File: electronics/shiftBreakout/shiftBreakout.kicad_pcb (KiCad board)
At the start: 2 copper layers, 94 x 49.5 mm, 45 parts, among them J1 Screw_Terminal_01x05, J10 Sensor C, J11 Sensor D, J2 Screw_Terminal_01x06, J3 Motor A, J4 Screw_Terminal_01x05, J5 Motor B, J6 Motor C, J7 Motor D, J8 Sensor A, J9 Sensor B, U1 74HC595, U2 TPL7407L, U3 74HC244, U4 74HC165, U5 74HC595, U6 TPL7407L, U7 74HC595, U8 TPL7407L

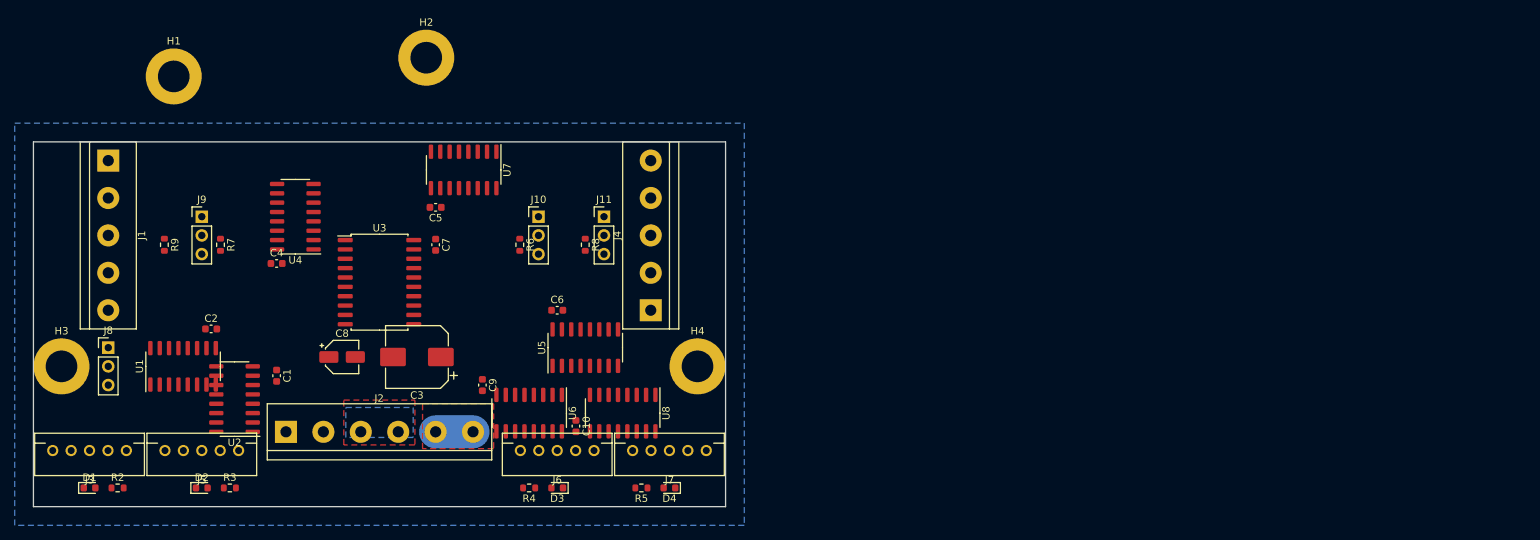
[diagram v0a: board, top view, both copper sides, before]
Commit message: Shift breakout PCB progress
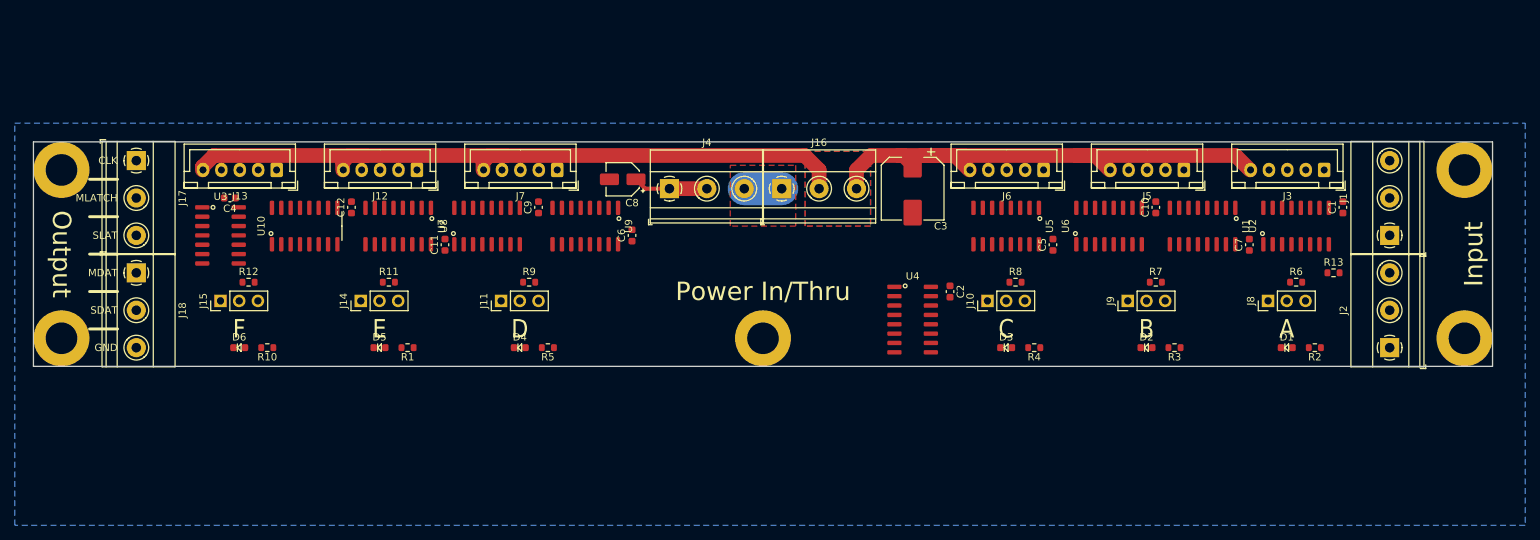
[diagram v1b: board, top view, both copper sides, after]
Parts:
- added C11: 0.1uF, Capacitor_SMD:C_0603_1608Metric, F.Cu at (81.3, 39.4)
- added C12: 0.1uF, Capacitor_SMD:C_0603_1608Metric, F.Cu at (68.6, 34.3)
- added D5: LED E, ModifiedSymbols:LED_0603_1608Metric_Silkscreen, F.Cu at (72.4, 53.3)
- added D6: LED F, ModifiedSymbols:LED_0603_1608Metric_Silkscreen, F.Cu at (53.3, 53.3)
- added H5: MountingHole, MountingHole:MountingHole_4.3mm_M4_ISO7380_Pad, F.Cu at (124.5, 52.1)
- added J12: Motor E, Connector_JST:JST_XH_B5B-XH-A_1x05_P2.50mm_Vertical, F.Cu at (77.5, 29.2)
- added J13: Motor F, Connector_JST:JST_XH_B5B-XH-A_1x05_P2.50mm_Vertical, F.Cu at (58.4, 29.2)
- added J14: Sensor E, Connector_PinHeader_2.54mm:PinHeader_1x03_P2.54mm_Vertical, F.Cu at (69.8, 47.0)
- added J15: Sensor F, Connector_PinHeader_2.54mm:PinHeader_1x03_P2.54mm_Vertical, F.Cu at (50.8, 47.0)
- added J16: PowerB, TerminalBlock_Phoenix:TerminalBlock_Phoenix_MKDS-1,5-3-5.08_1x03_P5.08mm_Horizontal, F.Cu at (127.0, 31.8)
- added J17: Outputs_A, TerminalBlock_Phoenix:TerminalBlock_Phoenix_MKDS-1,5-3-5.08_1x03_P5.08mm_Horizontal, F.Cu at (39.4, 27.9)
- added J18: Outputs_B, TerminalBlock_Phoenix:TerminalBlock_Phoenix_MKDS-1,5-3-5.08_1x03_P5.08mm_Horizontal, F.Cu at (39.4, 43.2)
- added R1: 220R, Resistor_SMD:R_0603_1608Metric, F.Cu at (76.2, 53.3)
- added R10: 220R, Resistor_SMD:R_0603_1608Metric, F.Cu at (57.1, 53.3)
- added R11: 47k, Resistor_SMD:R_0603_1608Metric, F.Cu at (73.7, 44.5)
- added R12: 47k, Resistor_SMD:R_0603_1608Metric, F.Cu at (54.6, 44.5)
- added R13: 0R, Resistor_SMD:R_0603_1608Metric, F.Cu at (201.9, 43.2)
- added U10: TPL7407L, ModifiedSymbols:SOIC-16_3.9x9.9mm_P1.27mm_silk, F.Cu at (62.2, 36.8)
- added U9: 74HC595, ModifiedSymbols:SOIC-16_3.9x9.9mm_P1.27mm_silk, F.Cu at (100.3, 36.8)
- D1, D2, D3, D4: footprint LED_SMD:LED_0603_1608Metric -> ModifiedSymbols:LED_0603_1608Metric_Silkscreen
- J1: value Screw_Terminal_01x05 -> Inputs_B; footprint TerminalBlock:TerminalBlock_bornier-5_P5.08mm -> TerminalBlock_Phoenix:TerminalBlock_Phoenix_MKDS-1,5-3-5.08_1x03_P5.08mm_Horizontal
- J2: value Screw_Terminal_01x06 -> Input_A; footprint TerminalBlock:TerminalBlock_bornier-6_P5.08mm -> TerminalBlock_Phoenix:TerminalBlock_Phoenix_MKDS-1,5-3-5.08_1x03_P5.08mm_Horizontal
- J3, J5, J6, J7: footprint JST_XH_Connectors:JST_XH_2-5mm_5pin -> Connector_JST:JST_XH_B5B-XH-A_1x05_P2.50mm_Vertical
- J4: value Screw_Terminal_01x05 -> PowerA; footprint TerminalBlock:TerminalBlock_bornier-5_P5.08mm -> TerminalBlock_Phoenix:TerminalBlock_Phoenix_MKDS-1,5-3-5.08_1x03_P5.08mm_Horizontal
- U1, U2, U4, U5, U6, U7, U8: footprint Package_SO:SOIC-16_3.9x9.9mm_P1.27mm -> ModifiedSymbols:SOIC-16_3.9x9.9mm_P1.27mm_silk
- U3: value 74HC244 -> 74HC125; footprint Package_SO:SOIC-20W_7.5x12.8mm_P1.27mm -> ModifiedSymbols:SOIC-14_3.9x8.7mm_P1.27mm_silk
- moved J1 174.3 mm to (209.6, 38.1), turned to 90 degrees
- moved J3 171.9 mm to (200.7, 29.2), turned to 180 degrees
- moved D1 163.7 mm to (195.6, 53.3)
- moved R2 163.7 mm to (199.4, 53.3)
- moved J8 157.6 mm to (193.0, 47.0), turned to 90 degrees
- moved J2 150.3 mm to (209.6, 53.3), turned to 90 degrees
- moved C1 146.6 mm to (203.2, 34.3), turned to 90 degrees
- moved U2 146.0 mm to (196.8, 36.8), turned to 90 degrees
- moved H2 141.8 mm to (219.7, 29.2)
- moved U1 139.7 mm to (184.2, 36.8), turned to 270 degrees
- moved J5 138.7 mm to (181.6, 29.2), turned to 180 degrees
- moved D2 129.7 mm to (176.5, 53.3)
- moved R3 129.7 mm to (180.3, 53.3)
- moved R7 127.1 mm to (177.8, 44.5), turned to 0 degrees
- moved J9 126.2 mm to (174.0, 47.0), turned to 90 degrees
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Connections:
- J1 pad 1: GND -> /SENSOR_LATCH_IN
- J1 pad 2: (no net) -> /MOTOR_LATCH_IN
- J1 pad 3: /MOTOR_IN -> /CLOCK_IN
- J2 pad 1: +3V3 -> GND
- J2 pad 2: +3V3 -> /SENSOR_OUT
- J2 pad 3: GND -> /MOTOR_IN
- J4 pad 1: (no net) -> +3V3
- J4 pad 2: (no net) -> +3V3
- J4 pad 3: (no net) -> GND
- U1 pad 12: /LATCH_IN -> /MOTOR_LATCH_IN
- U3 pad 11: (no net) -> /MOTOR_OUT
- U3 pad 12: (no net) -> /MOTOR_OUT_PRE_BUFFER
- U3 pad 13: (no net) -> GND
- U3 pad 14: (no net) -> +3V3
- U3 pad 2: (no net) -> /CLOCK_IN
- U3 pad 3: (no net) -> /CLOCK_OUT
- U3 pad 4: (no net) -> GND
- U3 pad 5: (no net) -> /MOTOR_LATCH_IN
- U3 pad 6: (no net) -> /MOTOR_LATCH_OUT
- U3 pad 7: (no net) -> GND
- U3 pad 8: (no net) -> /SENSOR_LATCH_OUT
- U3 pad 9: (no net) -> /SENSOR_LATCH_IN
- U4 pad 1: /LATCH_IN -> /SENSOR_LATCH_IN
- U4 pad 10: (no net) -> /SENSOR_IN
- U4 pad 3: /LOOPBACK_A -> /SENSOR_E
- U4 pad 4: /LOOPBACK_B -> /SENSOR_F
- U4 pad 5: /LOOPBACK_C -> /LOOPBACK_A
- U4 pad 6: /LOOPBACK_D -> /LOOPBACK_B
- U4 pad 9: (no net) -> /SENSOR_OUT
- U5 pad 12: /LATCH_IN -> /MOTOR_LATCH_IN
- U5 pad 4: /MOTOR_D_PHASE_A -> /LED_A
- U5 pad 5: /MOTOR_D_PHASE_B -> /LED_B
- U5 pad 6: /MOTOR_D_PHASE_C -> /LED_C
- U5 pad 7: /MOTOR_D_PHASE_D -> /LOOPBACK_A
- U7 pad 1: /LED_B -> /MOTOR_E_PHASE_B
- U7 pad 12: /LATCH_IN -> /MOTOR_LATCH_IN
- U7 pad 14: Net-(U5-Pad9) -> Net-(U7-Pad14)
- U7 pad 15: /LED_A -> /MOTOR_E_PHASE_A
- U7 pad 2: /LED_C -> /MOTOR_E_PHASE_C
- U7 pad 3: /LED_D -> /MOTOR_E_PHASE_D
- U7 pad 4: /LOOPBACK_A -> /MOTOR_F_PHASE_A
- U7 pad 5: /LOOPBACK_B -> /MOTOR_F_PHASE_B
- U7 pad 6: /LOOPBACK_C -> /MOTOR_F_PHASE_C
- U7 pad 7: /LOOPBACK_D -> /MOTOR_F_PHASE_D
- U7 pad 9: (no net) -> /MOTOR_OUT_PRE_BUFFER
- U8 pad 1: /MOTOR_D_PHASE_D -> /MOTOR_E_PHASE_B
- U8 pad 11: (no net) -> /OUT_D_PHASE_A
- U8 pad 12: (no net) -> /OUT_D_PHASE_B
- U8 pad 13: /OUT_D_PHASE_A -> /OUT_D_PHASE_C
- U8 pad 14: /OUT_D_PHASE_B -> /OUT_D_PHASE_D
- U8 pad 15: /OUT_D_PHASE_C -> /OUT_E_PHASE_A
- U8 pad 16: /OUT_D_PHASE_D -> /OUT_E_PHASE_B
- U8 pad 2: /MOTOR_D_PHASE_C -> /MOTOR_E_PHASE_A
- U8 pad 3: /MOTOR_D_PHASE_B -> /MOTOR_D_PHASE_D
- U8 pad 4: /MOTOR_D_PHASE_A -> /MOTOR_D_PHASE_C
- U8 pad 5: GND -> /MOTOR_D_PHASE_B
- U8 pad 6: GND -> /MOTOR_D_PHASE_A
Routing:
- net +12V: track 5.08 -> 171.0 mm
- net +3V3: track 0.00 -> 10.2 mm
- net GND: track 0.00 -> 5.08 mm
- added copper zone on B.Cu, net +12V
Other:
- board size 94 x 49.5 mm -> 198.1 x 30.5 mm
- board text added: "A"
- board text added: "B"
- board text added: "C"
- board text added: "CLK"
- board text added: "D"
- board text added: "E"
- board text added: "F"
- board text added: "GND"
- board text added: "Input"
- board text added: "MDAT"
- board text added: "MLATCH"
- board text added: "Output"
- board text added: "Power In/Thru"
- board text added: "SDAT"
- board text added: "SLAT"

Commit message: Finished shiftBreakout PCB
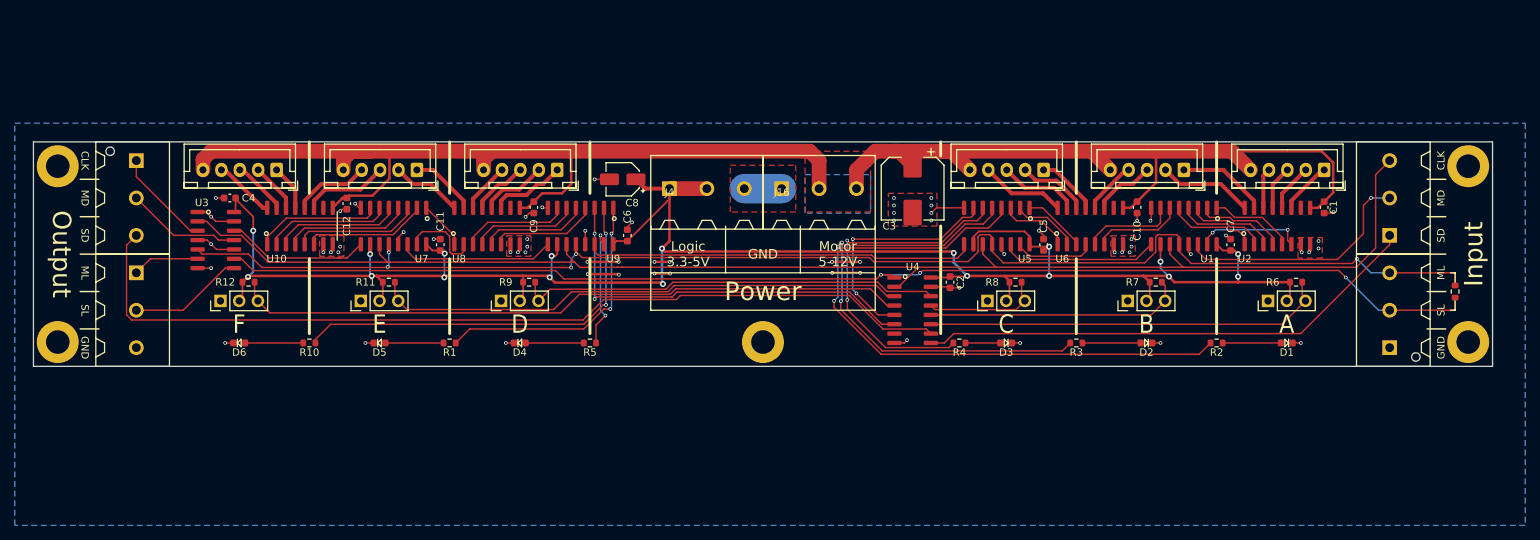
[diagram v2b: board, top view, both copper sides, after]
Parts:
- added H6: MountingHole, JLCPCB:AssemblyToolingHole, F.Cu at (35.8, 26.7)
- added H7: MountingHole, JLCPCB:AssemblyToolingHole, F.Cu at (213.1, 54.6)
- H1, H2, H3, H4, H5: footprint MountingHole:MountingHole_4.3mm_M4_ISO7380_Pad -> MountingHole:MountingHole_3.2mm_M3_ISO7380_Pad
- J1, J17, J18: footprint TerminalBlock_Phoenix:TerminalBlock_Phoenix_MKDS-1,5-3-5.08_1x03_P5.08mm_Horizontal -> ScrewTerminals:C72334_WJ500V-5.08-3P
- J16: value PowerB -> Power_B; footprint TerminalBlock_Phoenix:TerminalBlock_Phoenix_MKDS-1,5-3-5.08_1x03_P5.08mm_Horizontal -> ScrewTerminals:C72334_WJ500V-5.08-3P
- J2: value Input_A -> Inputs_A; footprint TerminalBlock_Phoenix:TerminalBlock_Phoenix_MKDS-1,5-3-5.08_1x03_P5.08mm_Horizontal -> ScrewTerminals:C72334_WJ500V-5.08-3P
- J4: value PowerA -> Power_A; footprint TerminalBlock_Phoenix:TerminalBlock_Phoenix_MKDS-1,5-3-5.08_1x03_P5.08mm_Horizontal -> ScrewTerminals:C72334_WJ500V-5.08-3P
- moved R13 16.7 mm to (218.4, 45.7), turned to 90 degrees
- moved R3 13.4 mm to (167.0, 52.7), turned to 180 degrees
- moved R2 13.4 mm to (186.1, 52.7), turned to 180 degrees
- moved R4 10.2 mm to (151.1, 52.7), turned to 180 degrees
- moved R1 5.75 mm to (81.9, 52.7)
- moved R10 5.75 mm to (62.9, 52.7)
- moved R5 5.75 mm to (101.0, 52.7)
- moved C10 2.54 mm to (175.3, 34.3)
- moved C1 2.54 mm to (200.7, 34.3)
- moved C7 2.54 mm to (188.0, 39.4)
- moved U1 2.54 mm to (181.6, 36.8)
- moved U2 2.54 mm to (194.3, 36.8)
- moved U6 2.54 mm to (168.9, 36.8)
- moved C5 1.27 mm to (162.6, 39.4)
- moved U4 1.27 mm to (144.8, 48.3)
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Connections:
- J1 pad 1: /SENSOR_LATCH_IN -> /SENSOR_OUT
- J1 pad 2: /MOTOR_LATCH_IN -> /MOTOR_IN
- J17 pad 2: /MOTOR_LATCH_OUT -> /MOTOR_OUT
- J17 pad 3: /SENSOR_LATCH_OUT -> /SENSOR_IN
- J18 pad 1: /MOTOR_OUT -> /MOTOR_LATCH_OUT
- J18 pad 2: /SENSOR_IN -> /SENSOR_LATCH_OUT
- J2 pad 2: /SENSOR_OUT -> /SENSOR_LATCH_IN
- J2 pad 3: /MOTOR_IN -> /MOTOR_LATCH_IN
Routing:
- net +3V3: track 10.2 -> 267.1 mm, vias 0 -> 18
- net /CLOCK_IN: track 0.00 -> 196.4 mm
- net /MOTOR_LATCH_IN: track 0.00 -> 193.0 mm, vias 0 -> 5
- net /SENSOR_LATCH_IN: track 0.00 -> 173.4 mm, vias 0 -> 3
- net /SENSOR_IN: track 0.00 -> 124.4 mm
- net /SENSOR_F: track 0.00 -> 92.1 mm
- net /LED_A: track 0.00 -> 88.0 mm, vias 0 -> 2
- net GND: track 5.08 -> 78.3 mm, vias 0 -> 66
- net /SENSOR_E: track 0.00 -> 72.5 mm
- net /SENSOR_OUT: track 0.00 -> 69.1 mm
- net /LED_B: track 0.00 -> 66.3 mm, vias 0 -> 2
- net /SENSOR_D: track 0.00 -> 57.8 mm
- net /LOOPBACK_B: track 0.00 -> 55.3 mm, vias 0 -> 2
- net +12V: track 171.0 -> 226.3 mm
- net /LED_F: track 0.00 -> 55.2 mm, vias 0 -> 2
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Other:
- net class Default: clearance 0.2 -> 0.15; trace_width 0.25 -> 0.2; via_dia 0.8 -> 0.5; via_drill 0.4 -> 0.3
- net class save added: clearance 0.2, trace_width 0.25, via_dia 0.8, via_drill 0.4
- rule trace_clearance: 0.2 -> 0.15
- rule trace_min: 0.2 -> 0.127
- rule via_min_drill: 0.3 -> 0.2
- rule via_min_size: 0.4 -> 0.45
- board text added: "ID#"
- board text added: "JLCJLCJLCJLC"
- board text added: "Logic 3.3-5V"
- board text added: "MD"
- board text added: "ML"
- board text added: "Motor 5-12V"
- board text added: "Power"
- board text added: "SD"
- board text added: "SL"
- board text added: "Splitflap Chainlink Driver"
- board text added: "[alpha]"
- board text added: "https://github.com/scottbez1/splitflap"
- board text removed: "MDAT"
- board text removed: "MLATCH"
- board text removed: "Power In/Thru"
- board text removed: "SDAT"
- board text removed: "SLAT"

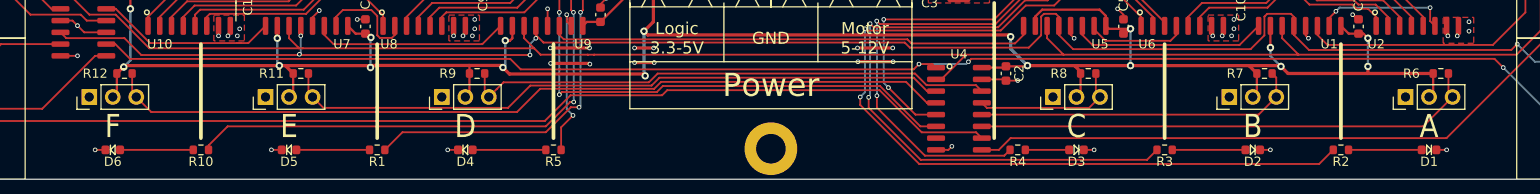
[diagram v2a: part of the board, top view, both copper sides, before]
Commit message: Add polarity markings for sensor connectors, remove JLC order number placeholder
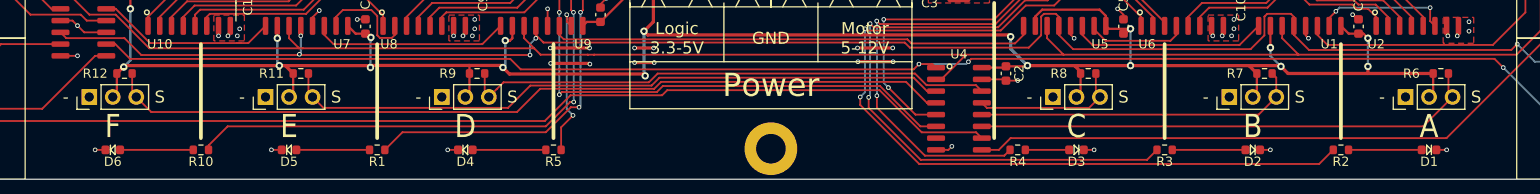
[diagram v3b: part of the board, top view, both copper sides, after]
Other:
- board text added: "-"
- board text added: "S"
- board text removed: "JLCJLCJLCJLC"
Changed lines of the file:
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@@
   (general
     (thickness 1.6)
-    (drawings 68)
+    (drawings 79)
     (tracks 811)
     (zones 0)
@@
   )
   (setup
-    (last_trace_width 0.35)
+    (last_trace_width 0.2)
     (user_trace_width 0.15)
     (user_trace_width 0.35)
@@
     )
   )
+  (gr_text - (at 48.26 46.99) (layer F.SilkS)
+    (effects (font (size 1.3 1.3) (thickness 0.15)))
+  )
+  (gr_text S (at 58.42 46.99) (layer F.SilkS)
+    (effects (font (size 1.3 1.3) (thickness 0.15)))
+  )
+  (gr_text S (at 77.47 46.99) (layer F.SilkS)
+    (effects (font (size 1.3 1.3) (thickness 0.15)))
+  )
+  (gr_text - (at 67.31 46.99) (layer F.SilkS)
+    (effects (font (size 1.3 1.3) (thickness 0.15)))
+  )
+  (gr_text - (at 86.36 46.99) (layer F.SilkS)
+    (effects (font (size 1.3 1.3) (thickness 0.15)))
+  )
+  (gr_text S (at 96.52 46.99) (layer F.SilkS)
+    (effects (font (size 1.3 1.3) (thickness 0.15)))
+  )
+  (gr_text S (at 162.56 46.99) (layer F.SilkS)
+    (effects (font (size 1.3 1.3) (thickness 0.15)))
+  )
+  (gr_text - (at 152.4 46.99) (layer F.SilkS)
+    (effects (font (size 1.3 1.3) (thickness 0.15)))
+  )
+  (gr_text - (at 171.45 46.99) (layer F.SilkS)
+    (effects (font (size 1.3 1.3) (thickness 0.15)))
+  )
+  (gr_text S (at 181.61 46.99) (layer F.SilkS)
+    (effects (font (size 1.3 1.3) (thickness 0.15)))
+  )
+  (gr_text S (at 200.66 46.99) (layer F.SilkS)
+    (effects (font (size 1.3 1.3) (thickness 0.15)))
+  )
+  (gr_text - (at 190.5 46.99) (layer F.SilkS)
+    (effects (font (size 1.3 1.3) (thickness 0.15)))
+  )
   (gr_text https://github.com/scottbez1/splitflap (at 203.454 36.322) (layer B.SilkS)
     (effects (font (size 1.5 1.5) (thickness 0.12)) (justify left mirror))
@@
   )
   (gr_poly (pts (xy 141.605 46.99) (xy 107.315 46.99) (xy 107.315 36.83) (xy 141.605 36.83)) (layer B.SilkS) (width 0.1))
-  (gr_text JLCJLCJLCJLC (at 48.768 53.086) (layer B.SilkS)
-    (effects (font (size 0.8 0.8) (thickness 0.15)) (justify mirror))
-  )
   (gr_line (start 148.59 36.83) (end 148.59 51.435) (layer F.SilkS) (width 0.4))
   (gr_line (start 148.59 25.4) (end 148.59 27.305) (layer F.SilkS) (width 0.4))

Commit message: Add templates for date/commit; move dimensions to comments layer
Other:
- board text added: "DATE: YYYY-MM-DD COMMIT: deadbeef"
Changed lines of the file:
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@@
   (general
     (thickness 1.6)
-    (drawings 79)
+    (drawings 80)
     (tracks 811)
     (zones 0)
@@
     )
   )
+  (gr_text "DATE: YYYY-MM-DD\nCOMMIT: deadbeef" (at 203.835 52.07) (layer B.SilkS)
+    (effects (font (size 1.2 1.2) (thickness 0.12)) (justify left mirror))
+  )
   (gr_text - (at 48.26 46.99) (layer F.SilkS)
     (effects (font (size 1.3 1.3) (thickness 0.15)))
@@
   (gr_line (start 25.4 55.88) (end 25.4 25.4) (layer Edge.Cuts) (width 0.05))
   (gr_line (start 223.52 25.4) (end 223.52 55.88) (layer Edge.Cuts) (width 0.05))
-  (dimension 198.12 (width 0.15) (layer F.SilkS)
-    (gr_text "198.120 mm" (at 124.46 16.48) (layer F.SilkS)
+  (dimension 198.12 (width 0.15) (layer Cmts.User)
+    (gr_text "198.120 mm" (at 124.46 16.48) (layer Cmts.User)
       (effects (font (size 1 1) (thickness 0.15)))
     )
@@
     (arrow2b (pts (xy 25.4 17.78) (xy 26.526504 17.193579)))
   )
-  (dimension 30.48 (width 0.15) (layer F.SilkS)
-    (gr_text "30.480 mm" (at 16.48 40.64 -90) (layer F.SilkS)
+  (dimension 30.48 (width 0.15) (layer Cmts.User)
+    (gr_text "30.480 mm" (at 16.48 40.64 -90) (layer Cmts.User)
       (effects (font (size 1 1) (thickness 0.15)))
     )
